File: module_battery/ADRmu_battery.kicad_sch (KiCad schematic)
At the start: 51 parts, among them J101 Harting 09042326831, Q101 Q_NMOS_GDS, Q102 Q_NMOS_GDS, U101 BQ7791500, U102 LM317_TO-263

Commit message: Battery module Rev 0.2
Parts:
- removed D?: 1N4001, Diode_THT:D_DO-41_SOD81_P10.16mm_Horizontal, symbol Diode:1N4001
- removed R121: 1R4 2W, Resistor_SMD:R_2512_6332Metric, symbol Device:R
- removed U102: LM317_TO-263, Package_TO_SOT_SMD:TO-263-2, symbol Regulator_Linear:LM317_TO-263
- added R116: 9.1M, Resistor_SMD:R_0805_2012Metric, symbol Device:R
- added R117: 680k, Resistor_SMD:R_0805_2012Metric, symbol Device:R
- added R123: 10k, Resistor_SMD:R_0805_2012Metric, symbol Device:R
- added R124: 1k2, Resistor_SMD:R_0805_2012Metric, symbol Device:R
- added TH102: CMFB3435103FNT, Resistor_SMD:R_0805_2012Metric, symbol Device:Thermistor_NTC
- added U102: LTC4079, Package_DFN_QFN:DFN-10-1EP_3x3mm_P0.5mm_EP1.65x2.38mm, symbol ADRmu_battery_Library:LTC4079
- R122: renamed from R120; value 16k9 -> 49k9
- R125: renamed from R122; value 16k9 -> 49k9
- TH101: value Thermistor_NTC -> CMFB3435103FNT
- renumbered H102 to H101, H101 to H102, H104 to H103, H103 to H104, R116 to R118, R117 to R119, R118 to R120, R119 to R121
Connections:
- net +BATT: now also R116.2, U102.10 (BAT)
- net -i/o: now also C112.1, J101.a24 (Pin_a24), J101.c24 (Pin_c24), R124.1, TH102.1, U102.11 (GND), U102.6 (TIMER)
- net GND: no longer C112.1, D104.1 (K), J101.a24 (Pin_a24), J101.c24 (Pin_c24)
- net in+: now also U102.1 (VDD), U102.2 (EN)
- new net: R124.2, U102.3 (PROG)
- new net: R123.2, U102.4 (NTCBIAS)
- new net: R123.1, TH102.2, U102.5 (NTC)
- new net: D104.1 (K), U102.7 (~{CHRG})
- new net: R117.1, U102.8 (FBG)
- new net: R116.1, R117.2, U102.9 (FB)
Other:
- moved on the sheet: B101A, B101B, B101C, B101D, C101, C102, C103, C104, C105, C106, C107, C108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

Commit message: asdf
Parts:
- added C112: 100n 50V, Capacitor_SMD:C_0805_2012Metric, symbol Device:C
- added C113, C115: 220u 16V, Capacitor_THT:CP_Radial_D10.0mm_P5.00mm, symbol Device:C_Polarized
- added U103: L7812, Package_TO_SOT_SMD:TO-252-2, symbol Regulator_Linear:L7812
- NT101: now left out of the parts list
- renumbered C112 to C114, R118 to R116, R119 to R117, R120 to R118, R121 to R119, R122 to R120, R116 to R121, R117 to R122
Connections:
- net +BATT: now also C112.2, U103.1 (IN); no longer J101.a2 (Pin_a2), J101.c2 (Pin_c2)
- net -i/o: now also C112.1, C113.2, C115.2, U103.2 (GND)
- net in+: now also C115.1
- new net: C113.1, J101.a2 (Pin_a2), J101.c2 (Pin_c2), U103.3 (OUT)

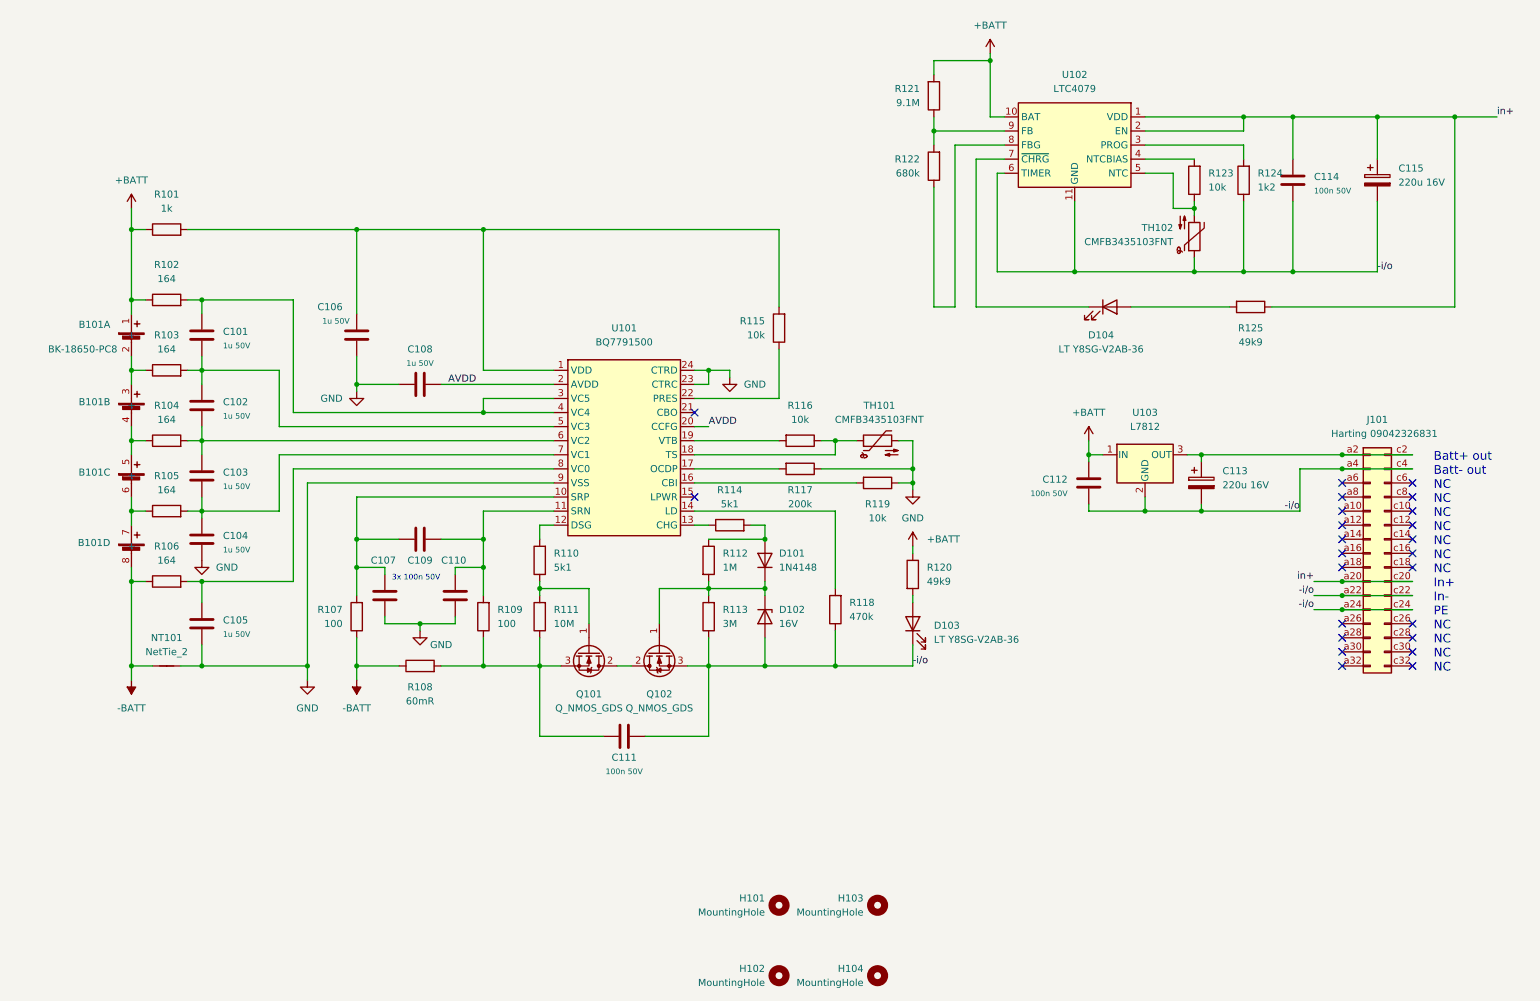
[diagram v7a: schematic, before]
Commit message: prepared rev 0.3 battery module with fuel gauge
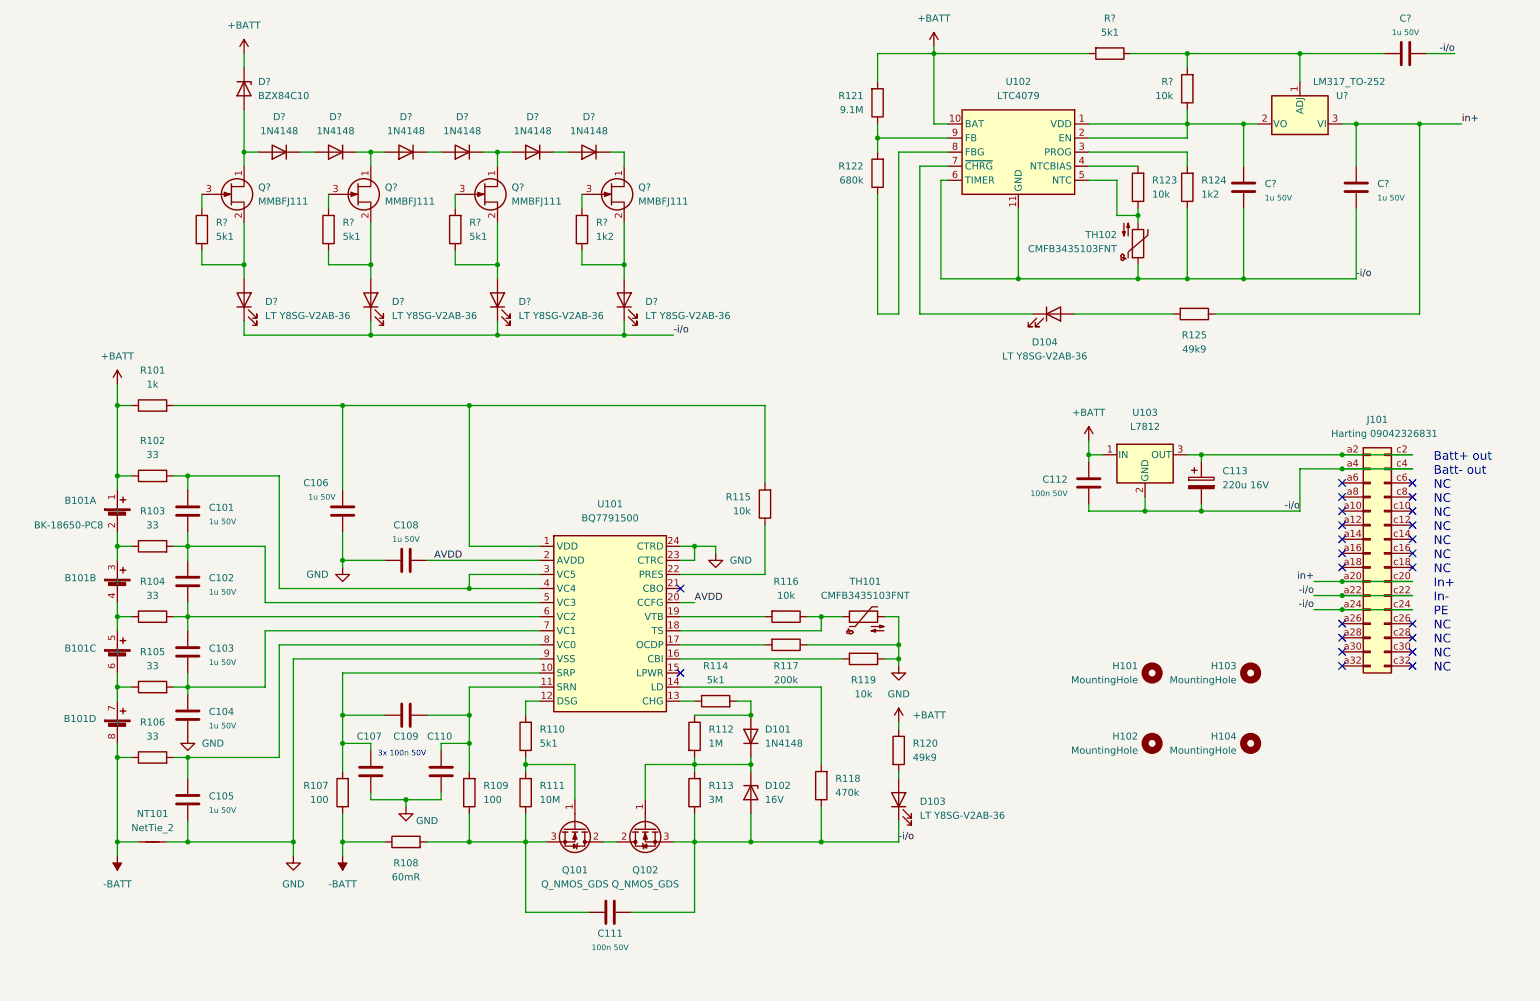
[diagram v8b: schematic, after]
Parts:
- removed C114: 100n 50V, Capacitor_SMD:C_0805_2012Metric, symbol Device:C
- removed C115: 220u 16V, Capacitor_THT:CP_Radial_D10.0mm_P5.00mm, symbol Device:C_Polarized
- added C? (x3): 1u 50V, Capacitor_SMD:C_0805_2012Metric, symbol Device:C
- added D? (x6): 1N4148, Diode_SMD:D_SOD-123, symbol Device:D
- added D? (x4): LT Y8SG-V2AB-36, LED_SMD:LED_1206_3216Metric, symbol Device:LED
- added D?: BZX84C10, Package_TO_SOT_SMD:SOT-23, symbol Diode:BZX84Cxx
- added Q? (x4): MMBFJ111, Package_TO_SOT_SMD:SOT-23, symbol Transistor_FET:MMBFJ111
- added R? (x4): 5k1, Resistor_SMD:R_0805_2012Metric, symbol Device:R
- added R?: 10k, Resistor_SMD:R_0805_2012Metric, symbol Device:R
- added R?: 1k2, Resistor_SMD:R_0805_2012Metric, symbol Device:R
- added U?: LM317_TO-252, Package_TO_SOT_SMD:TO-252-2, symbol Regulator_Linear:LM317_TO-252
- R102, R103, R104, R105, R106: value 164 -> 33
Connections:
- net +BATT: now also D?.3 (K), R?.2
- net -i/o: now also C?.2, C?.2, C?.2, D?.1 (K), D?.1 (K), D?.1 (K), D?.1 (K)
- net in+: now also C?.1, U?.3 (VI); no longer U102.1 (VDD), U102.2 (EN)
- new net: D?.2 (A), Q?.2 (S), R?.1 (x4)
- new net: Q?.3 (G), R?.2 (x4)
- new net: D?.1 (K), D?.2 (A) (x3)
- new net: D?.1 (A), D?.2 (A), Q?.1 (D)
- new net: C?.1, R?.1, R?.2, U?.1 (ADJ)
- new net: C?.1, R?.1, U102.1 (VDD), U102.2 (EN), U?.2 (VO)
- new net: D?.1 (K), D?.2 (A), Q?.1 (D) (x2)
- new net: D?.1 (K), Q?.1 (D)
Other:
- moved on the sheet: B101A, B101B, B101C, B101D, C101, C102, C103, C104, C105, C106, C107, C108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
